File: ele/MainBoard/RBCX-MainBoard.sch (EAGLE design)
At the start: 313 parts, among them IC1 AMS1117-3.3, IC10 INA180A4, IC11 INA180A4, IC2 DRV8833PWP, IC3 INA180A4, IC4 INA180A4, IC5 DRV8833PWP, IC6 INA180A4, IC7 INA180A4, IC8 INA180A4, IC9 INA180A4, Q1 CHOOSE_ME, Q10 CHOOSE_ME, Q11 CHOOSE_ME, Q2 CHOOSE_ME, Q3 CHOOSE_ME, Q4 CHOOSE_ME, Q5 CHOOSE_ME, Q6 CHOOSE_ME, Q7 CHOOSE_ME, Q8 CHOOSE_ME, Q9 CHOOSE_ME, SW1 CHOOSE_ME, SW2 CHOOSE_ME, SW3 CHOOSE_ME, SW4 CHOOSE_ME, SW5 CHOOSE_ME, SW6 CHOOSE_ME, U1 STM32F103VCT6, X1 POWER_OUT, X10 52745-3090, X11 52745-2090, X2 POWER_IN, X3 M3B, X4 M4B, X5 M3B, X6 M4B, Y1 5032/2P, Y2 3215_2P

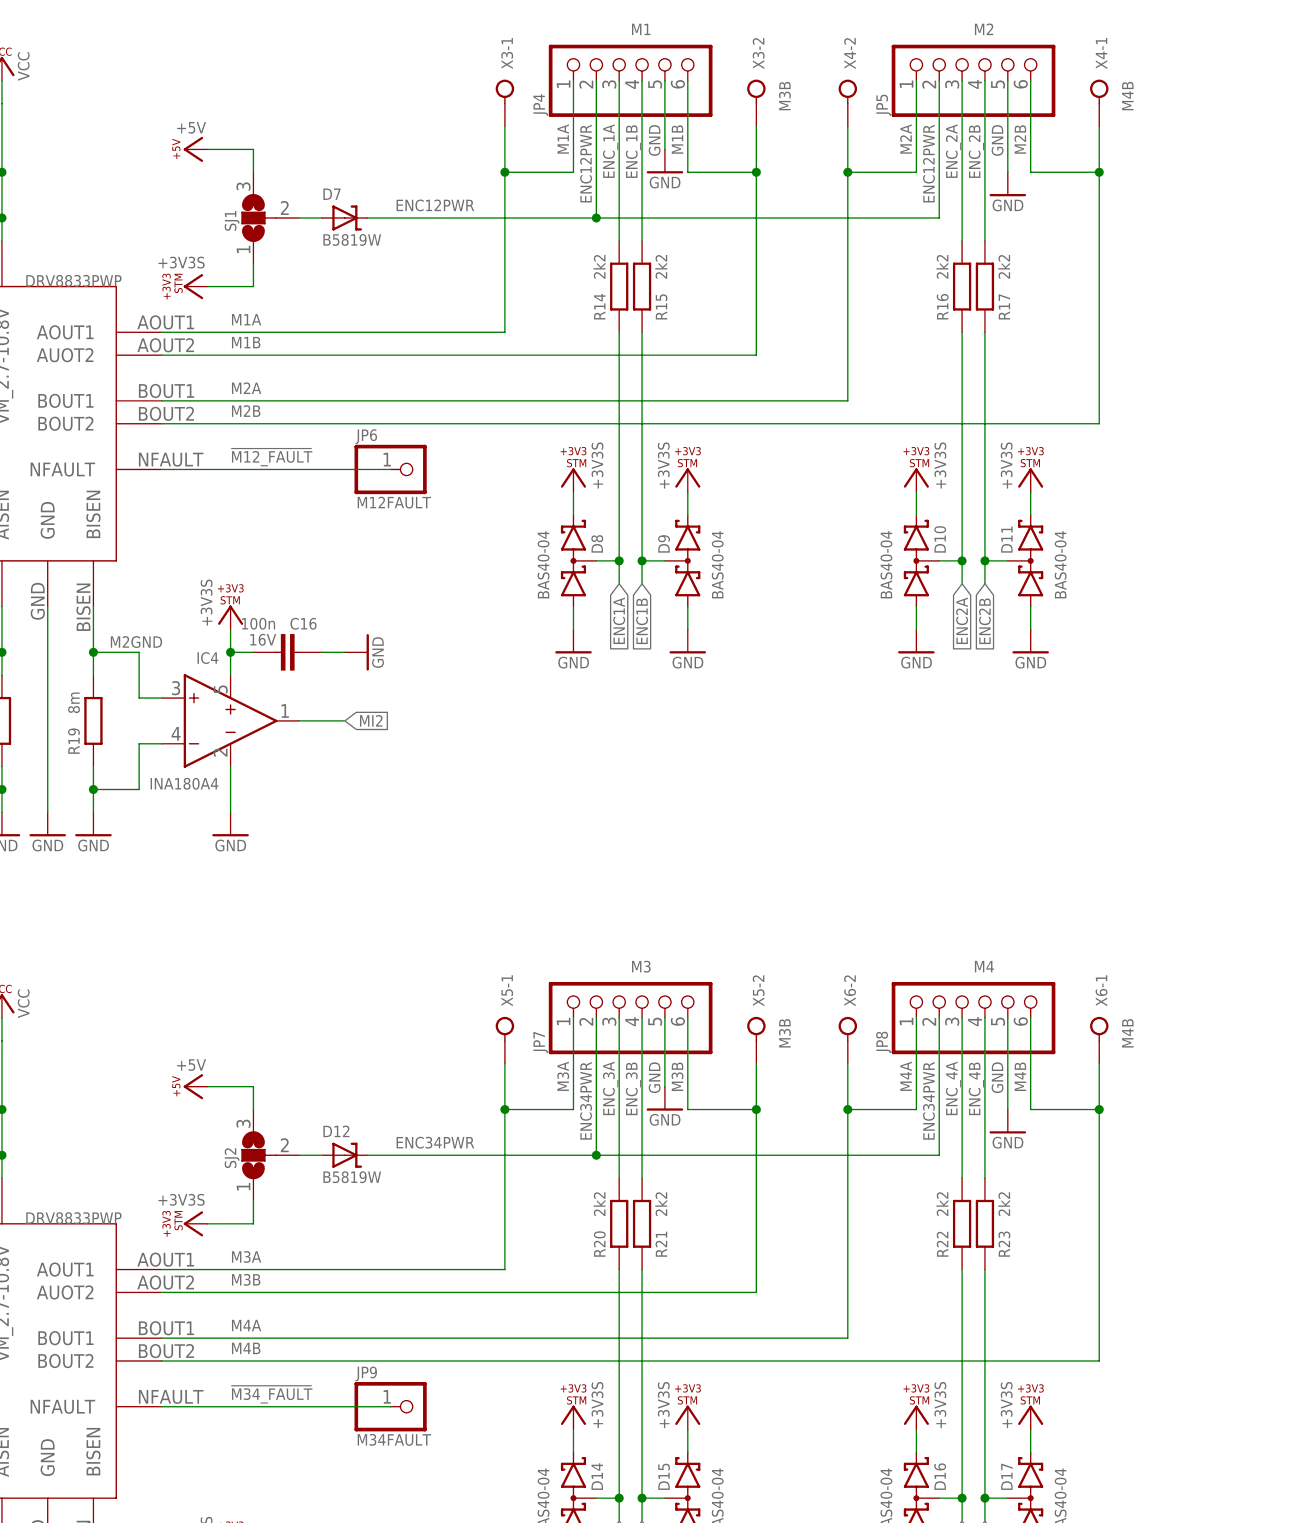
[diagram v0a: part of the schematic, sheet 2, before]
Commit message: MainBoard: Remove motors terminal block, leave only pinheads
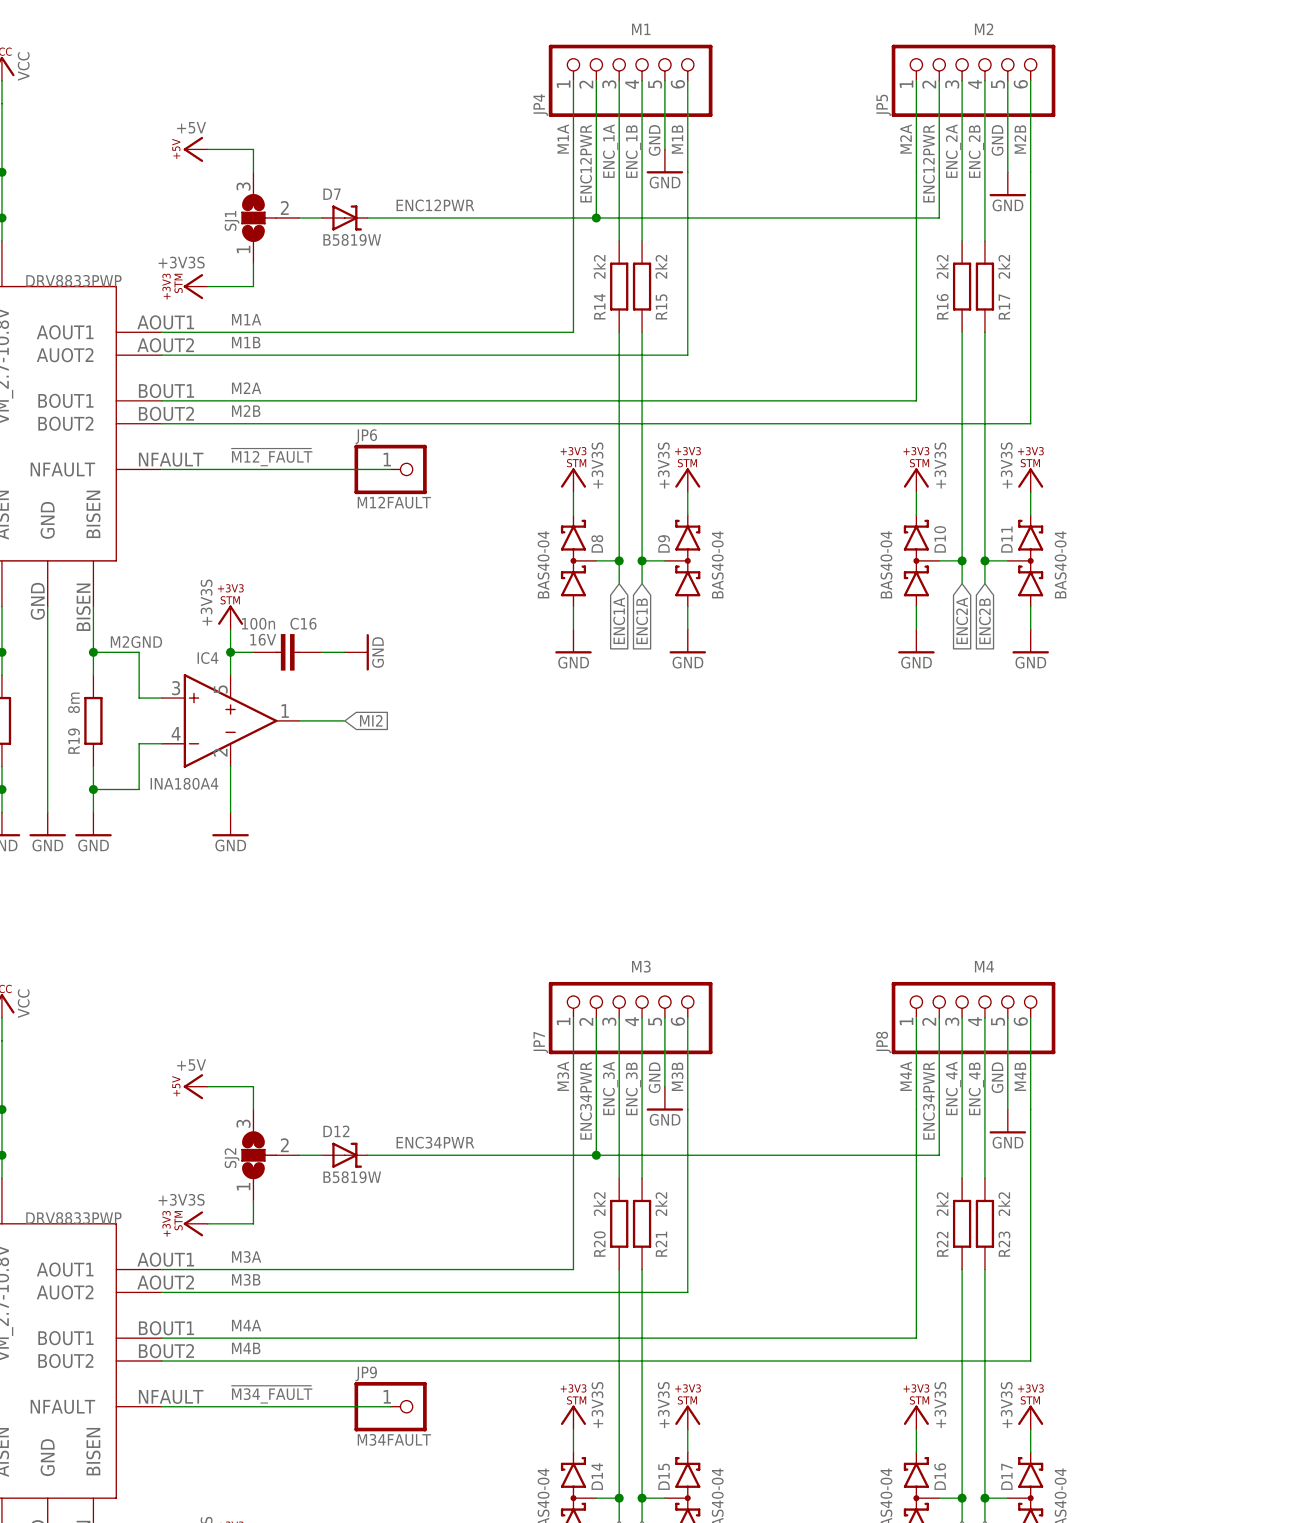
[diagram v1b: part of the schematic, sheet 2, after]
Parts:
- removed X3, X5: M3B, con-wago-508:W237-02P
- removed X4, X6: M4B, con-wago-508:W237-02P
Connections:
- net M1A: no longer X3-1.KL
- net M1B: no longer X3-2.KL
- net M2A: no longer X4-2.KL
- net M2B: no longer X4-1.KL
- net M3A: no longer X5-1.KL
- net M3B: no longer X5-2.KL
- net M4A: no longer X6-2.KL
- net M4B: no longer X6-1.KL

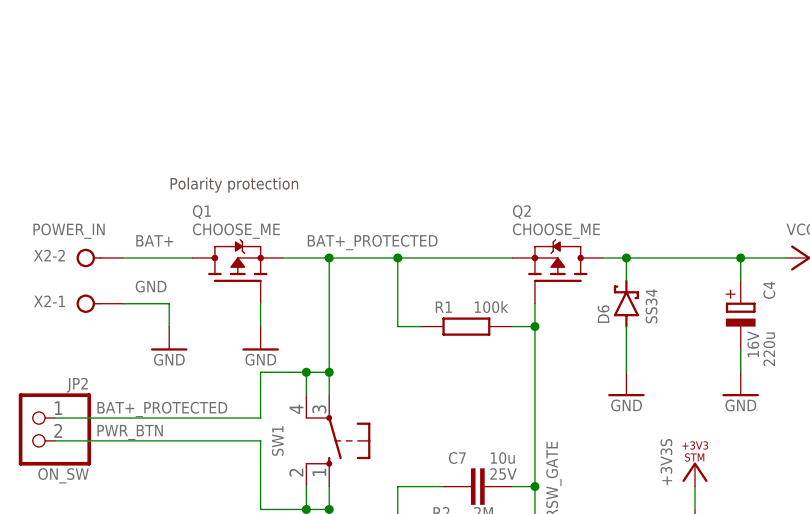
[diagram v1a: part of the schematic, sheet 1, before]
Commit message: MainBoard: Add P channel power MOSFETs value
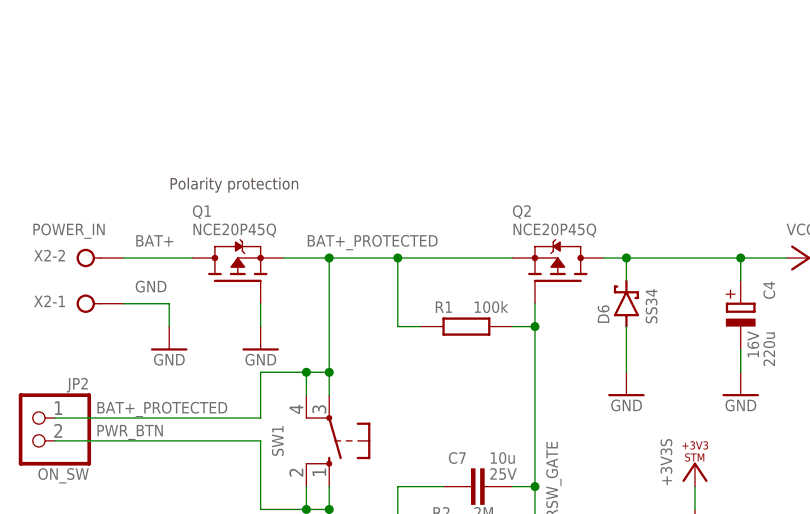
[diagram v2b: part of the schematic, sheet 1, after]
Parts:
- Q1, Q2: value CHOOSE_ME -> NCE20P45Q; DESCRIPTION (none) -> P MOSFET 19V 35A 7mΩ; LCSC_ID (none) -> C193354; MF_ID (none) -> NCE20P45Q; PACKAGE (none) -> DFN-8_EP_3.3x3.3x0.65P; PRICE_1000PLUS (none) -> $0.1218; PRICE_100PLUS (none) -> $0.1276; PRICE_10PLUS (none) -> $0.1450; PRICE_1PLUS (none) -> $0.1928; PRICE_30PLUS (none) -> $0.1363; PRICE_500PLUS (none) -> $0.1232
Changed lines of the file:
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@@
 </part>
 <part name="D6" library="diode" deviceset="BAT60J" device="DO-214-AB" package3d_urn="urn:adsk.eagle:package:43453/2" value="SS34"/>
-<part name="Q1" library="transistors" deviceset="P-MOSFET" device="-MLP_HS" value="CHOOSE_ME"/>
-<part name="Q2" library="transistors" deviceset="P-MOSFET" device="-MLP_HS" value="CHOOSE_ME"/>
+<part name="Q1" library="transistors" deviceset="P-MOSFET" device="-MLP_HS" value="NCE20P45Q">
+<attribute name="DESCRIPTION" value="P MOSFET 19V 35A 7mΩ"/>
+<attribute name="LCSC_ID" value="C193354"/>
+<attribute name="MF_ID" value="NCE20P45Q"/>
+<attribute name="PACKAGE" value="DFN-8_EP_3.3x3.3x0.65P"/>
+<attribute name="PRICE_1000PLUS" value="$0.1218"/>
+<attribute name="PRICE_100PLUS" value="$0.1276"/>
+<attribute name="PRICE_10PLUS" value="$0.1450"/>
+<attribute name="PRICE_1PLUS" value="$0.1928"/>
+<attribute name="PRICE_30PLUS" value="$0.1363"/>
+<attribute name="PRICE_500PLUS" value="$0.1232"/>
+</part>
 <part name="LED1" library="led" library_urn="urn:adsk.eagle:library:259" deviceset="LED" device="SML0603" package3d_urn="urn:adsk.eagle:package:15832/1" value="GREEN"/>
 <part name="Y1" library="SMD5032_2P" deviceset="5032/2P" device=""/>
@@
 <part name="+3V26" library="Supply" deviceset="+3V3S" device=""/>
 <part name="GND104" library="Supply" deviceset="GND" device=""/>
+<part name="Q2" library="transistors" deviceset="P-MOSFET" device="-MLP_HS" value="NCE20P45Q">
+<attribute name="DESCRIPTION" value="P MOSFET 19V 35A 7mΩ"/>
+<attribute name="LCSC_ID" value="C193354"/>
+<attribute name="MF_ID" value="NCE20P45Q"/>
+<attribute name="PACKAGE" value="DFN-8_EP_3.3x3.3x0.65P"/>
+<attribute name="PRICE_1000PLUS" value="$0.1218"/>
+<attribute name="PRICE_100PLUS" value="$0.1276"/>
+<attribute name="PRICE_10PLUS" value="$0.1450"/>
+<attribute name="PRICE_1PLUS" value="$0.1928"/>
+<attribute name="PRICE_30PLUS" value="$0.1363"/>
+<attribute name="PRICE_500PLUS" value="$0.1232"/>
+</part>
 </parts>
 <sheets>
@@
 <attribute name="VALUE" x="68.58" y="175.26" size="1.27" layer="96"/>
 <attribute name="NAME" x="68.58" y="177.292" size="1.27" layer="95"/>
-</instance>
-<instance part="Q2" gate="G$1" x="109.22" y="170.18" smashed="yes" rot="R90">
-<attribute name="VALUE" x="104.14" y="175.26" size="1.27" layer="96"/>
-<attribute name="NAME" x="104.14" y="177.292" size="1.27" layer="95"/>
+<attribute name="DESCRIPTION" x="73.66" y="170.18" size="1.27" layer="96" rot="MR90" display="off"/>
+<attribute name="LCSC_ID" x="73.66" y="170.18" size="1.27" layer="96" rot="MR90" display="off"/>
+<attribute name="MF_ID" x="73.66" y="170.18" size="1.27" layer="96" rot="MR90" display="off"/>
+<attribute name="PACKAGE" x="73.66" y="170.18" size="1.27" layer="96" rot="MR90" display="off"/>
+<attribute name="PRICE_1000PLUS" x="73.66" y="170.18" size="1.27" layer="96" rot="MR90" display="off"/>
+<attribute name="PRICE_100PLUS" x="73.66" y="170.18" size="1.27" layer="96" rot="MR90" display="off"/>
+<attribute name="PRICE_10PLUS" x="73.66" y="170.18" size="1.27" layer="96" rot="MR90" display="off"/>
+<attribute name="PRICE_1PLUS" x="73.66" y="170.18" size="1.27" layer="96" rot="MR90" display="off"/>
+<attribute name="PRICE_30PLUS" x="73.66" y="170.18" size="1.27" layer="96" rot="MR90" display="off"/>
+<attribute name="PRICE_500PLUS" x="73.66" y="170.18" size="1.27" layer="96" rot="MR90" display="off"/>
 </instance>
 <instance part="SW1" gate="1" x="83.82" y="152.4" smashed="yes" rot="R180">
@@
 <attribute name="VALUE" x="57.15" y="149.352" size="1.27" layer="96" rot="R180"/>
 </instance>
+<instance part="Q2" gate="G$1" x="109.22" y="170.18" smashed="yes" rot="R90">
+<attribute name="VALUE" x="104.14" y="175.26" size="1.27" layer="96"/>
+<attribute name="NAME" x="104.14" y="177.292" size="1.27" layer="95"/>
+<attribute name="DESCRIPTION" x="109.22" y="170.18" size="1.27" layer="96" rot="R90" display="off"/>
+<attribute name="LCSC_ID" x="109.22" y="170.18" size="1.27" layer="96" rot="R90" display="off"/>
+<attribute name="MF_ID" x="109.22" y="170.18" size="1.27" layer="96" rot="R90" display="off"/>
+<attribute name="PACKAGE" x="109.22" y="170.18" size="1.27" layer="96" rot="R90" display="off"/>
+<attribute name="PRICE_1000PLUS" x="109.22" y="170.18" size="1.27" layer="96" rot="R90" display="off"/>
+<attribute name="PRICE_100PLUS" x="109.22" y="170.18" size="1.27" layer="96" rot="R90" display="off"/>
+<attribute name="PRICE_10PLUS" x="109.22" y="170.18" size="1.27" layer="96" rot="R90" display="off"/>
+<attribute name="PRICE_1PLUS" x="109.22" y="170.18" size="1.27" layer="96" rot="R90" display="off"/>
+<attribute name="PRICE_30PLUS" x="109.22" y="170.18" size="1.27" layer="96" rot="R90" display="off"/>
+<attribute name="PRICE_500PLUS" x="109.22" y="170.18" size="1.27" layer="96" rot="R90" display="off"/>
+</instance>
 </instances>
 <busses>
@@
 <label x="81.28" y="173.99" size="1.27" layer="95"/>
 <pinref part="Q1" gate="G$1" pin="S"/>
-<pinref part="Q2" gate="G$1" pin="S"/>
 <pinref part="R1" gate="G$1" pin="1"/>
 <wire x1="93.98" y1="165.1" x2="91.44" y2="165.1" width="0.1524" layer="91"/>
@@
 <wire x1="81.28" y1="157.48" x2="81.28" y2="160.02" width="0.1524" layer="91"/>
 <junction x="81.28" y="160.02"/>
+<pinref part="Q2" gate="G$1" pin="S"/>
 </segment>
 </net>
@@
 <pinref part="R1" gate="G$1" pin="2"/>
 <wire x1="104.14" y1="165.1" x2="106.68" y2="165.1" width="0.1524" layer="91"/>
-<pinref part="Q2" gate="G$1" pin="G"/>
 <wire x1="106.68" y1="165.1" x2="106.68" y2="167.64" width="0.1524" layer="91"/>
 <pinref part="Q5" gate="G$1" pin="D"/>
@@
 <pinref part="R2" gate="G$1" pin="2"/>
 <pinref part="C7" gate="G$1" pin="1"/>
+<pinref part="Q2" gate="G$1" pin="G"/>
 </segment>
 </net>
@@
 <segment>
 <wire x1="114.3" y1="172.72" x2="116.84" y2="172.72" width="0.1524" layer="91"/>
-<pinref part="Q2" gate="G$1" pin="D"/>
 <pinref part="P+1" gate="VCC" pin="VCC"/>
 <pinref part="D6" gate="G$1" pin="C"/>
@@
 <wire x1="129.54" y1="170.18" x2="129.54" y2="172.72" width="0.1524" layer="91"/>
 <junction x="129.54" y="172.72"/>
-</segment>
-<segment>
+<pinref part="Q2" gate="G$1" pin="D"/>
+</segment>
+<segment>

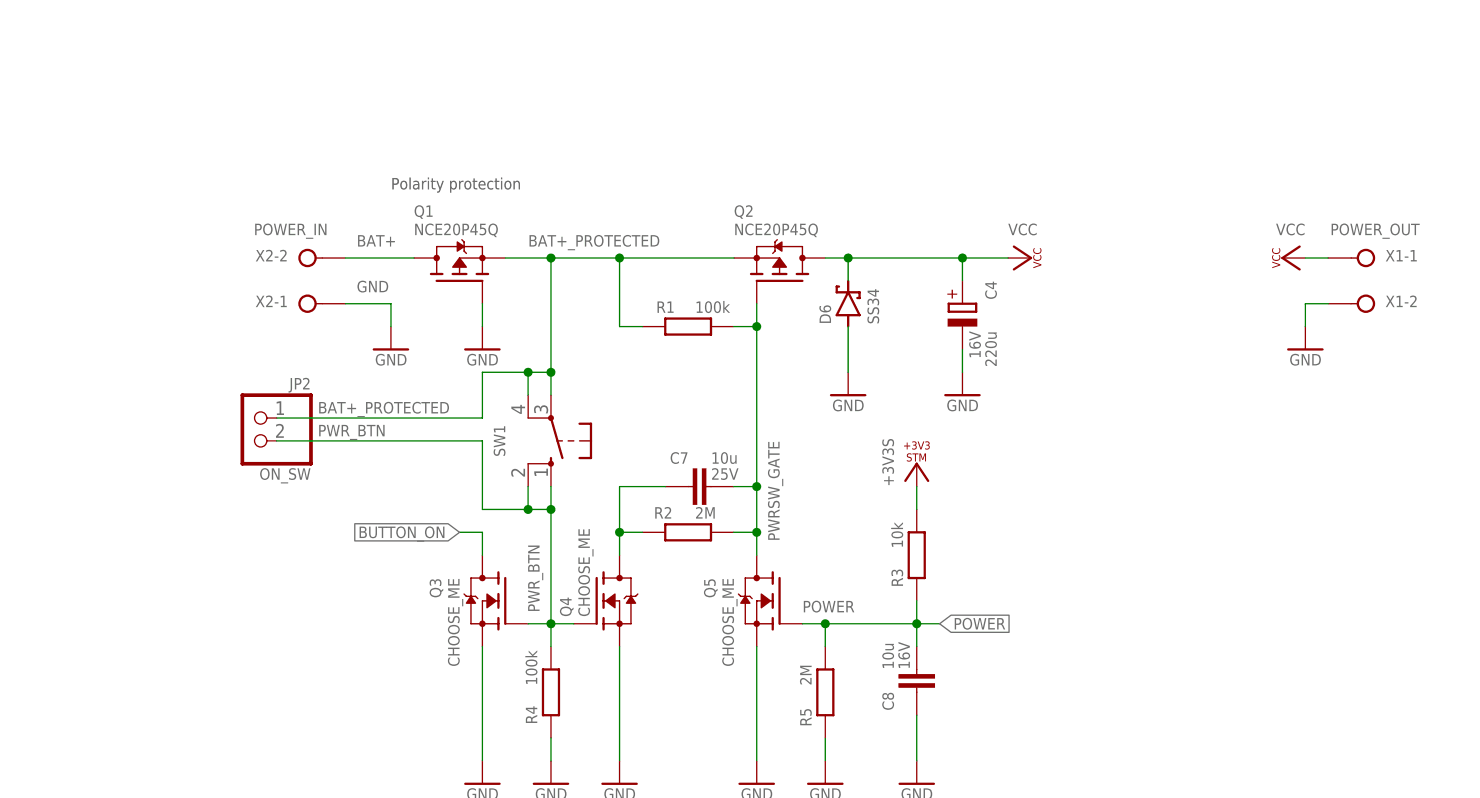
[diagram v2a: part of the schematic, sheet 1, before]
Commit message: MainBoardSCH: Add P channel power MOSFETs gate voltage spikes protection
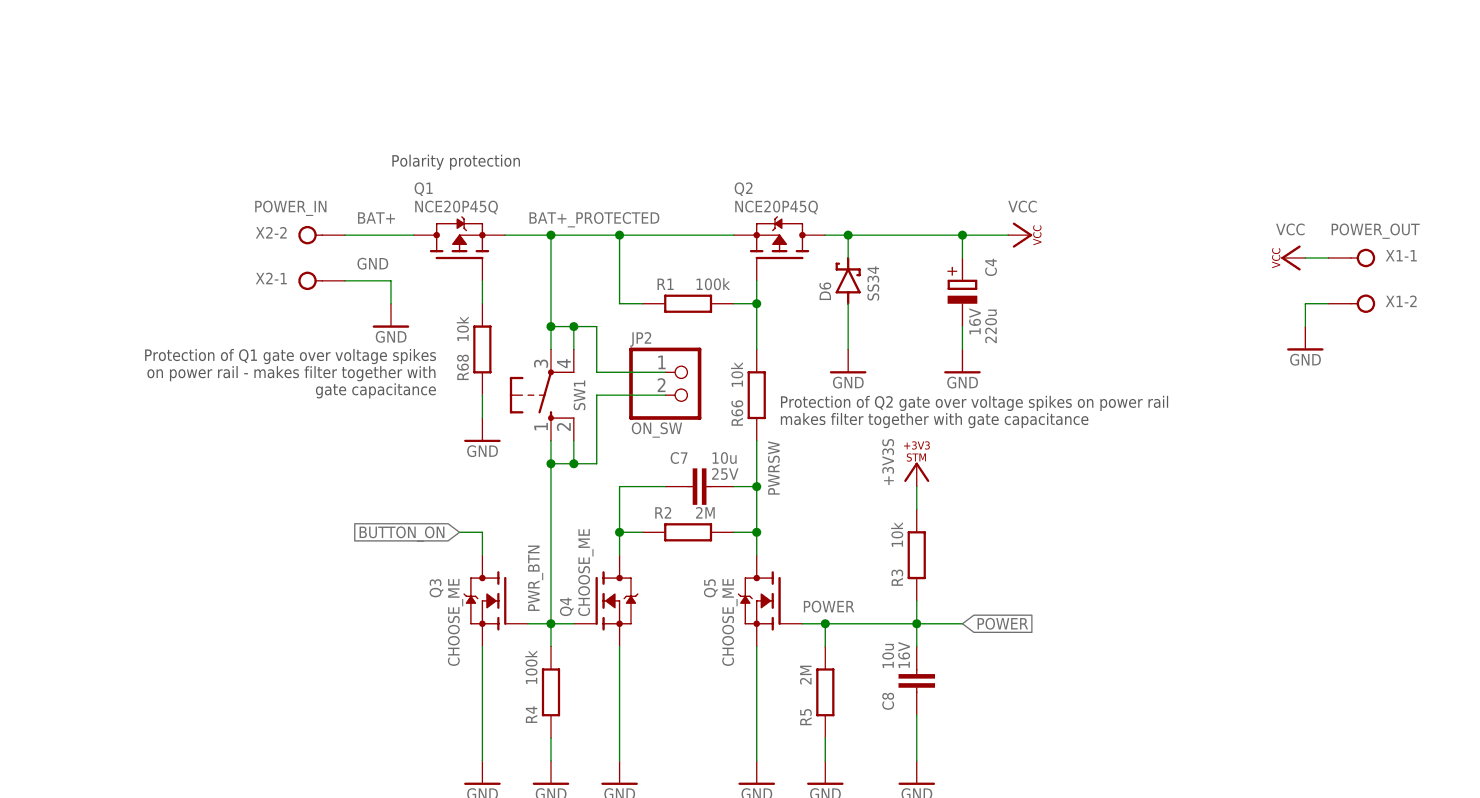
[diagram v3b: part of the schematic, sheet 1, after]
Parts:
- added R66, R68: 10k, rcl_upravena:R-EU_R0603
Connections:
- net N$1 renamed VBAT/2
- new net PROT_GATE: Q1.G, R68.2
- new net PWRSW: C7.1, Q5.D, R2.2, R66.1
- net GND: now also R68.1; no longer Q1.G
- net PWRSW_GATE: now also R66.2; no longer C7.1, Q5.D, R2.2
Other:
- note added: "Protection of Q1 gate over voltage spikes on power rail - makes filter together with gate capacitance"
- note added: "Protection of Q2 gate over voltage spikes on power rail makes filter together with gate capacitance"
- moved on the sheet: C4, D6, JP2, Q1, Q2, R1, SW1, X2-1, X2-2
